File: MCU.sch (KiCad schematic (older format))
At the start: 17 parts, among them J6 GS2, U4 STM32F103CBTx, Y1 Crystal

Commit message: 完成したのでしばらく寝かせる
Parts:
- D11: footprint Diodes_SMD:D_SOD-323_HandSoldering -> Diodes_SMD:D_SOD-323
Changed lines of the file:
@@
 F 0 "D11" H 10150 3650 50  0000 C CNN
 F 1 "D" H 10150 3450 50  0000 C CNN
-F 2 "Diodes_SMD:D_SOD-323_HandSoldering" H 10150 3550 50  0001 C CNN
+F 2 "Diodes_SMD:D_SOD-323" H 10150 3550 50  0001 C CNN
 F 3 "" H 10150 3550 50  0001 C CNN
 	1    10150 3550

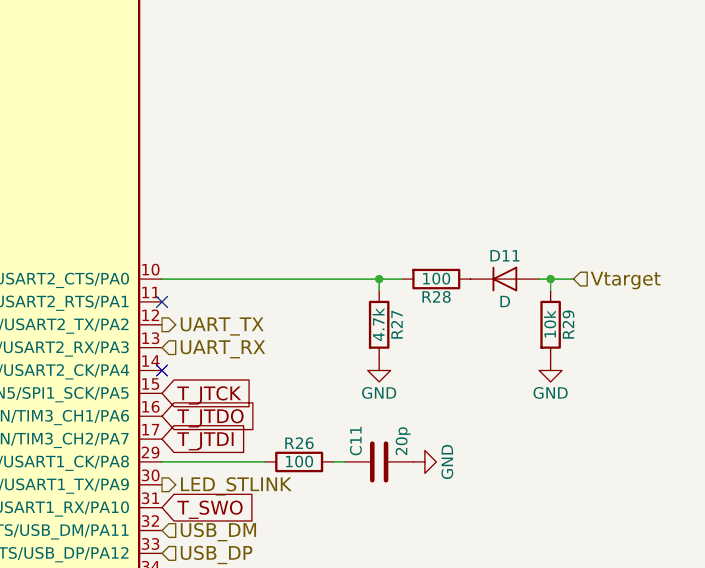
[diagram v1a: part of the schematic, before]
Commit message: ダンピング抵抗追加 分圧抵抗に変更
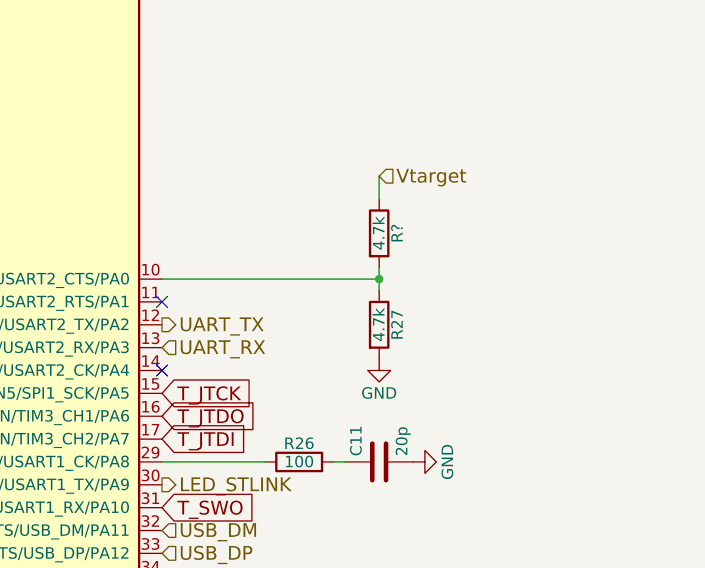
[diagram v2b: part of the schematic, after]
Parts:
- removed D11: D, Diodes_SMD:D_SOD-323, symbol D
- removed R28: 100, Resistors_SMD:R_0603, symbol R
- removed R29: 10k, Resistors_SMD:R_0603, symbol R
- added R?: 4.7k, Resistors_SMD:R_0603, symbol R
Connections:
- net Vtarget: now also R?.1
- net at R27.1, U4.10 (ADC1_IN0/ADC2_IN0/SYS_WKUP/TIM2_CH1/TIM2_ETR/USART2_CTS/PA0): now also R?.2
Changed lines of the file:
@@
 EESchema Schematic File Version 2
+LIBS:Isolate_ST-Link-rescue
 LIBS:power
 LIBS:device
@@
 	1    0    0    -1
 $EndComp
-$Comp
-L R R28
-U 1 1 59484A6F
-P 9850 3550
-F 0 "R28" V 9930 3550 50  0000 C CNN
-F 1 "100" V 9850 3550 50  0000 C CNN
-F 2 "Resistors_SMD:R_0603" V 9780 3550 50  0001 C CNN
-F 3 "" H 9850 3550 50  0001 C CNN
-	1    9850 3550
-	0    1    1    0
-$EndComp
-Wire Wire Line
-	8650 3550 9700 3550
-Wire Wire Line
-	9600 3600 9600 3550
+Wire Wire Line
+	9600 3500 9600 3600
 Connection ~ 9600 3550
 $Comp
@@
 	1    0    0    -1
 $EndComp
-$Comp
-L D D11
-U 1 1 59484C09
-P 10150 3550
-F 0 "D11" H 10150 3650 50  0000 C CNN
-F 1 "D" H 10150 3450 50  0000 C CNN
-F 2 "Diodes_SMD:D_SOD-323" H 10150 3550 50  0001 C CNN
-F 3 "" H 10150 3550 50  0001 C CNN
-	1    10150 3550
-	1    0    0    -1
-$EndComp
-$Comp
-L R R29
-U 1 1 59484D0E
-P 10350 3750
-F 0 "R29" V 10430 3750 50  0000 C CNN
-F 1 "10k" V 10350 3750 50  0000 C CNN
-F 2 "Resistors_SMD:R_0603" V 10280 3750 50  0001 C CNN
-F 3 "" H 10350 3750 50  0001 C CNN
-	1    10350 3750
-	1    0    0    -1
-$EndComp
-Wire Wire Line
-	10300 3550 10450 3550
-Wire Wire Line
-	10350 3550 10350 3600
-$Comp
-L GND #PWR054
-U 1 1 59484DB9
-P 10350 3900
-F 0 "#PWR054" H 10350 3650 50  0001 C CNN
-F 1 "GND" H 10350 3750 50  0000 C CNN
-F 2 "" H 10350 3900 50  0001 C CNN
-F 3 "" H 10350 3900 50  0001 C CNN
-	1    10350 3900
-	1    0    0    -1
-$EndComp
-Text HLabel 10450 3550 2    60   Input ~ 0
+Text HLabel 9600 3100 2    60   Input ~ 0
 Vtarget
-Connection ~ 10350 3550
+$Comp
+L R R?
+U 1 1 59CAAEE5
+P 9600 3350
+F 0 "R?" V 9680 3350 50  0000 C CNN
+F 1 "4.7k" V 9600 3350 50  0000 C CNN
+F 2 "Resistors_SMD:R_0603" V 9530 3350 50  0001 C CNN
+F 3 "" H 9600 3350 50  0001 C CNN
+	1    9600 3350
+	1    0    0    -1
+$EndComp
+Wire Wire Line
+	9600 3100 9600 3200
+Wire Wire Line
+	8650 3550 9600 3550
 $EndSCHEMATC

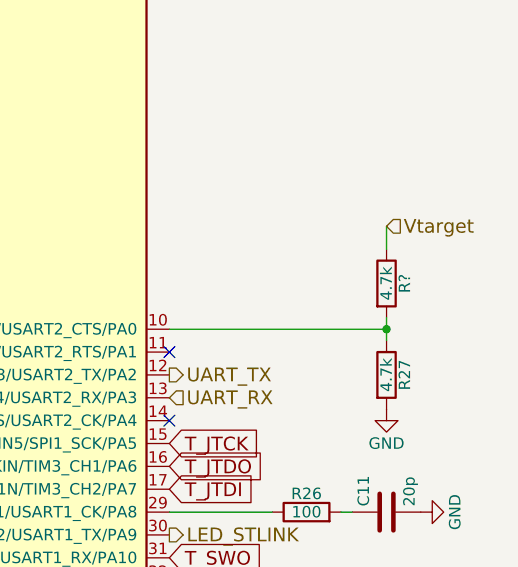
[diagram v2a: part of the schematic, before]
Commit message: 部品割当して基板の修正
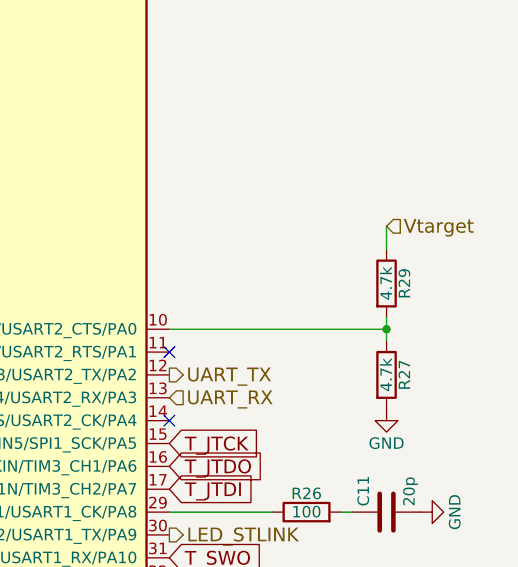
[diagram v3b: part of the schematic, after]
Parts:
- gave numbers to parts that had none: 1
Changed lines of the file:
@@
 Vtarget
 $Comp
-L R R?
+L R R29
 U 1 1 59CAAEE5
 P 9600 3350
-F 0 "R?" V 9680 3350 50  0000 C CNN
+F 0 "R29" V 9680 3350 50  0000 C CNN
 F 1 "4.7k" V 9600 3350 50  0000 C CNN
 F 2 "Resistors_SMD:R_0603" V 9530 3350 50  0001 C CNN

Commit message: https://github.com/Yuqlid/Isolate_ST-Link/projects/1#card-5148549 プルダウン抵抗追加
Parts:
- added R?: 10k, Resistors_SMD:R_0603, symbol R
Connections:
- net GND: now also R?.2
- net at J6.1 (G1), U4.39 (PB3/SPI1_SCK/SYS_JTDO-TRACESWO/TIM2_CH2): now also R?.1
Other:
- moved on the sheet: J6
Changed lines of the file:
@@
 L +3V3 #PWR051
 U 1 1 59481EA8
-P 2150 3850
-F 0 "#PWR051" H 2150 3700 50  0001 C CNN
-F 1 "+3V3" H 2150 3990 50  0000 C CNN
-F 2 "" H 2150 3850 50  0001 C CNN
-F 3 "" H 2150 3850 50  0001 C CNN
-	1    2150 3850
+P 1550 3850
+F 0 "#PWR051" H 1550 3700 50  0001 C CNN
+F 1 "+3V3" H 1550 3990 50  0000 C CNN
+F 2 "" H 1550 3850 50  0001 C CNN
+F 3 "" H 1550 3850 50  0001 C CNN
+	1    1550 3850
 	0    -1   -1   0
 $EndComp
@@
 L GS2 J6
 U 1 1 59481ED0
-P 2350 3850
-F 0 "J6" H 2450 4000 50  0000 C CNN
-F 1 "GS2" H 2450 3701 50  0000 C CNN
-F 2 "Connectors:GS2" V 2424 3850 50  0001 C CNN
-F 3 "" H 2350 3850 50  0001 C CNN
-	1    2350 3850
+P 1750 3850
+F 0 "J6" H 1850 4000 50  0000 C CNN
+F 1 "GS2" H 1850 3701 50  0000 C CNN
+F 2 "Connectors:GS2" V 1824 3850 50  0001 C CNN
+F 3 "" H 1750 3850 50  0001 C CNN
+	1    1750 3850
 	0    1    1    0
 $EndComp
 Wire Wire Line
-	2550 3850 2850 3850
+	1950 3850 2850 3850
 Text GLabel 8650 4050 2    60   Input ~ 0
 T_JTCK
@@
 Wire Wire Line
 	8650 3550 9600 3550
+$Comp
+L R R?
+U 1 1 59E3BD69
+P 2000 4050
+F 0 "R?" V 2080 4050 50  0000 C CNN
+F 1 "10k" V 2000 4050 50  0000 C CNN
+F 2 "Resistors_SMD:R_0603" V 1930 4050 50  0001 C CNN
+F 3 "" H 2000 4050 50  0001 C CNN
+	1    2000 4050
+	1    0    0    -1
+$EndComp
+$Comp
+L GND #PWR?
+U 1 1 59E3BDE9
+P 2000 4200
+F 0 "#PWR?" H 2000 3950 50  0001 C CNN
+F 1 "GND" H 2000 4050 50  0000 C CNN
+F 2 "" H 2000 4200 50  0001 C CNN
+F 3 "" H 2000 4200 50  0001 C CNN
+	1    2000 4200
+	1    0    0    -1
+$EndComp
+Wire Wire Line
+	2000 3900 2000 3850
+Connection ~ 2000 3850
 $EndSCHEMATC

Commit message: 修正
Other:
- moved on the sheet: C10, C11, C8, C9, J6, R21, R22, R23, R24, R25, R26, R27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

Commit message: 書き込みようの抵抗を追加
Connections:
- net SYS_JTMS: now reaches U4.34 (SYS_JTMS-SWDIO/PA13)
- net SYS_JTCK: now reaches U4.37 (SYS_JTCK-SWCLK/PA14)
- net SYS_NRST: now reaches C8.1, R21.2, U4.7 (NRST)
- no-connect marks 15 -> 13
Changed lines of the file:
@@
 $EndComp
 Wire Wire Line
-	1900 2300 1500 2300
+	1500 2300 2050 2300
 Wire Wire Line
 	1500 2250 1500 2350
@@
 Text HLabel 9150 5200 2    60   Input ~ 0
 USB_DP
-NoConn ~ 9150 5300
-NoConn ~ 9150 5400
 Text HLabel 9150 5500 2    60   Input ~ 0
 USB_RENUMn
@@
 	2500 4350 2500 4300
 Connection ~ 2500 4300
+Text GLabel 9750 5300 2    60   Input ~ 0
+SYS_JTMS
+Text GLabel 9750 5400 2    60   Input ~ 0
+SYS_JTCK
+Wire Wire Line
+	9750 5300 9150 5300
+Wire Wire Line
+	9150 5400 9750 5400
+Text GLabel 2050 2300 2    60   Input ~ 0
+SYS_NRST
+Connection ~ 1900 2300
 $EndSCHEMATC

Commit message: 進捗
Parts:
- gave numbers to parts that had none: 1
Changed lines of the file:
@@
 $EndComp
 $Comp
-L +3V3 #PWR042
+L +3V3 #PWR043
 U 1 1 5947EF34
 P 6050 2000
-F 0 "#PWR042" H 6050 1850 50  0001 C CNN
+F 0 "#PWR043" H 6050 1850 50  0001 C CNN
 F 1 "+3V3" H 6050 2140 50  0000 C CNN
 F 2 "" H 6050 2000 50  0001 C CNN
@@
 Connection ~ 6250 2200
 $Comp
-L +3V3 #PWR043
+L +3V3 #PWR044
 U 1 1 5947EFBD
 P 3350 3100
-F 0 "#PWR043" H 3350 2950 50  0001 C CNN
+F 0 "#PWR044" H 3350 2950 50  0001 C CNN
 F 1 "+3V3" H 3350 3240 50  0000 C CNN
 F 2 "" H 3350 3100 50  0001 C CNN
@@
 $EndComp
 $Comp
-L GND #PWR044
+L GND #PWR045
 U 1 1 5947F113
 P 1350 3350
-F 0 "#PWR044" H 1350 3100 50  0001 C CNN
+F 0 "#PWR045" H 1350 3100 50  0001 C CNN
 F 1 "GND" H 1350 3200 50  0000 C CNN
 F 2 "" H 1350 3350 50  0001 C CNN
@@
 Connection ~ 1950 3550
 $Comp
-L GND #PWR045
+L GND #PWR046
 U 1 1 5947F23B
 P 2850 2900
-F 0 "#PWR045" H 2850 2650 50  0001 C CNN
+F 0 "#PWR046" H 2850 2650 50  0001 C CNN
 F 1 "GND" H 2850 2750 50  0000 C CNN
 F 2 "" H 2850 2900 50  0001 C CNN
@@
 $EndComp
 $Comp
-L +3V3 #PWR046
+L +3V3 #PWR047
 U 1 1 5947F2A6
 P 1500 1950
-F 0 "#PWR046" H 1500 1800 50  0001 C CNN
+F 0 "#PWR047" H 1500 1800 50  0001 C CNN
 F 1 "+3V3" H 1500 2090 50  0000 C CNN
 F 2 "" H 1500 1950 50  0001 C CNN
@@
 $EndComp
 $Comp
-L GND #PWR047
+L GND #PWR048
 U 1 1 5947F407
 P 1500 2650
-F 0 "#PWR047" H 1500 2400 50  0001 C CNN
+F 0 "#PWR048" H 1500 2400 50  0001 C CNN
 F 1 "GND" H 1500 2500 50  0000 C CNN
 F 2 "" H 1500 2650 50  0001 C CNN
@@
 $EndComp
 $Comp
-L GND #PWR048
+L GND #PWR049
 U 1 1 594801AF
 P 2500 3700
-F 0 "#PWR048" H 2500 3450 50  0001 C CNN
+F 0 "#PWR049" H 2500 3450 50  0001 C CNN
 F 1 "GND" H 2500 3550 50  0000 C CNN
 F 2 "" H 2500 3700 50  0001 C CNN
@@
 NoConn ~ 9150 4400
 $Comp
-L GND #PWR049
+L GND #PWR050
 U 1 1 59480A30
 P 6050 6100
-F 0 "#PWR049" H 6050 5850 50  0001 C CNN
+F 0 "#PWR050" H 6050 5850 50  0001 C CNN
 F 1 "GND" H 6050 5950 50  0000 C CNN
 F 2 "" H 6050 6100 50  0001 C CNN
@@
 NoConn ~ 3350 4100
 $Comp
-L GND #PWR050
+L GND #PWR051
 U 1 1 59480F6D
 P 3350 4200
-F 0 "#PWR050" H 3350 3950 50  0001 C CNN
+F 0 "#PWR051" H 3350 3950 50  0001 C CNN
 F 1 "GND" H 3350 4050 50  0000 C CNN
 F 2 "" H 3350 4200 50  0001 C CNN
@@
 NoConn ~ 3350 4400
 $Comp
-L +3V3 #PWR051
+L +3V3 #PWR052
 U 1 1 59481EA8
 P 2050 4300
-F 0 "#PWR051" H 2050 4150 50  0001 C CNN
+F 0 "#PWR052" H 2050 4150 50  0001 C CNN
 F 1 "+3V3" H 2050 4440 50  0000 C CNN
 F 2 "" H 2050 4300 50  0001 C CNN
@@
 	9900 4800 9950 4800
 $Comp
-L GND #PWR052
+L GND #PWR053
 U 1 1 594827DF
 P 10250 4800
-F 0 "#PWR052" H 10250 4550 50  0001 C CNN
+F 0 "#PWR053" H 10250 4550 50  0001 C CNN
 F 1 "GND" H 10250 4650 50  0000 C CNN
 F 2 "" H 10250 4800 50  0001 C CNN
@@
 Connection ~ 10100 4000
 $Comp
-L GND #PWR053
+L GND #PWR054
 U 1 1 59484BA1
 P 10100 4350
-F 0 "#PWR053" H 10100 4100 50  0001 C CNN
+F 0 "#PWR054" H 10100 4100 50  0001 C CNN
 F 1 "GND" H 10100 4200 50  0000 C CNN
 F 2 "" H 10100 4350 50  0001 C CNN
@@
 	9150 4000 10100 4000
 $Comp
-L R R?
+L R R34
 U 1 1 59E3BD69
 P 2500 4500
-F 0 "R?" V 2580 4500 50  0000 C CNN
+F 0 "R34" V 2580 4500 50  0000 C CNN
 F 1 "10k" V 2500 4500 50  0000 C CNN
 F 2 "Resistors_SMD:R_0603" V 2430 4500 50  0001 C CNN
@@
 $EndComp
 $Comp
-L GND #PWR?
+L GND #PWR055
 U 1 1 59E3BDE9
 P 2500 4650
-F 0 "#PWR?" H 2500 4400 50  0001 C CNN
+F 0 "#PWR055" H 2500 4400 50  0001 C CNN
 F 1 "GND" H 2500 4500 50  0000 C CNN
 F 2 "" H 2500 4650 50  0001 C CNN
